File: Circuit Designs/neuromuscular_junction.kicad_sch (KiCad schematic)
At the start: 14 parts

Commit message: deleted previous version files
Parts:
- added R6: 3.3K, CoF_Resistor:R-0402, symbol CoE_Resistor:3.3K
- added R7, R8: 22R, CoF_Resistor:R-0402, symbol CoE_Resistor:22R
- C27, C28, C29, C30, C31, C32, C33: renamed from C?; footprint Capacitor_SMD:C_0402_1005Metric -> CoF_Capacitor:C-0402
- R1, R2, R3, R4, R5, R9: renamed from R?; footprint Resistor_SMD:R_0402_1005Metric -> CoF_Resistor:R-0402
- gave numbers to parts that had none: 1
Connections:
- net +3V3: now also R6.1
- net D+: now also R7.1
- net D-: now also R8.1
- new net USBD+: R6.2, R7.2
- new net USBD-: R8.2
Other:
- moved on the sheet: C33, R9

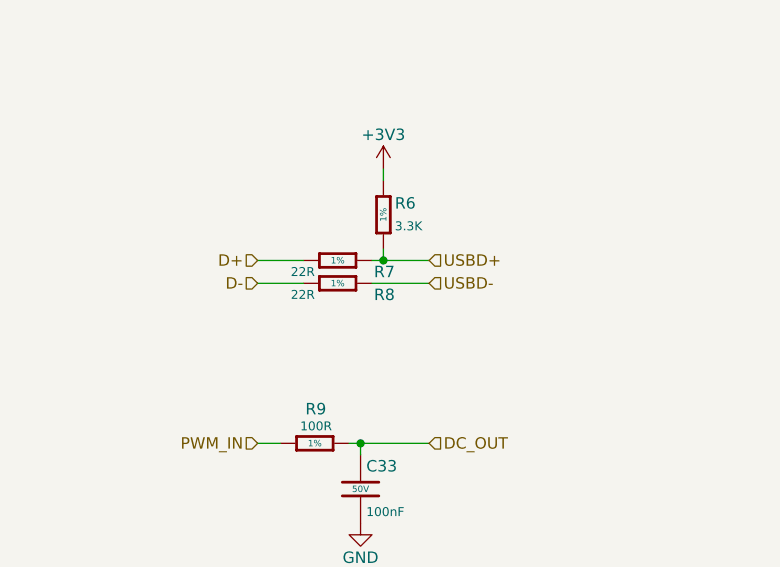
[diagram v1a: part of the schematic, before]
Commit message: changed the LED packages, edited field reference positions
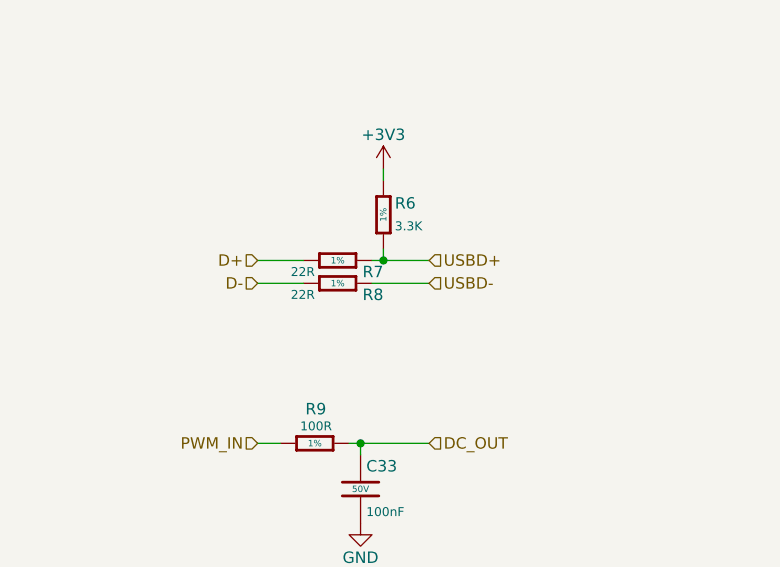
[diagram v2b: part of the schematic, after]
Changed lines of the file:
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@@
   (symbol (lib_id "CoE_Resistor:22R") (at 146.05 119.38 90) (unit 1)
     (in_bom yes) (on_board yes)
-    (property "Reference" "R7" (id 0) (at 152.4 120.65 90)
+    (property "Reference" "R7" (id 0) (at 151.13 120.65 90)
       (effects (font (size 1.27 1.27)) (justify left))
     )
@@
   (symbol (lib_id "CoE_Resistor:22R") (at 146.05 121.92 90) (unit 1)
     (in_bom yes) (on_board yes)
-    (property "Reference" "R8" (id 0) (at 152.4 123.19 90)
+    (property "Reference" "R8" (id 0) (at 151.13 123.19 90)
       (effects (font (size 1.27 1.27)) (justify left))
     )

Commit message: First placement of the MCU Page's components are done
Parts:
- U1: footprint Package_TO_SOT_SMD:TSOT-23-8 -> CoF_SmallOutline:TSOT-23-8
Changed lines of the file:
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@@
       (effects (font (size 0.9906 0.9906)) (justify left))
     )
-    (property "Footprint" "Package_TO_SOT_SMD:TSOT-23-8" (id 2) (at 144.78 27.94 0)
+    (property "Footprint" "CoF_SmallOutline:TSOT-23-8" (id 2) (at 144.78 27.94 0)
       (effects (font (size 1.27 1.27)) (justify bottom) hide)
     )
